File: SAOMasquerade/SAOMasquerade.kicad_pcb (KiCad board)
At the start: 2 copper layers, 31.8 x 35.6 mm, 20 parts, among them Q1 BSS138, SW1 SW_DIP_x07, U1 CH32V003FxPx, U2 74LVC1G86, U3 74LVC1G38, X1 SAO, X2 BADGE

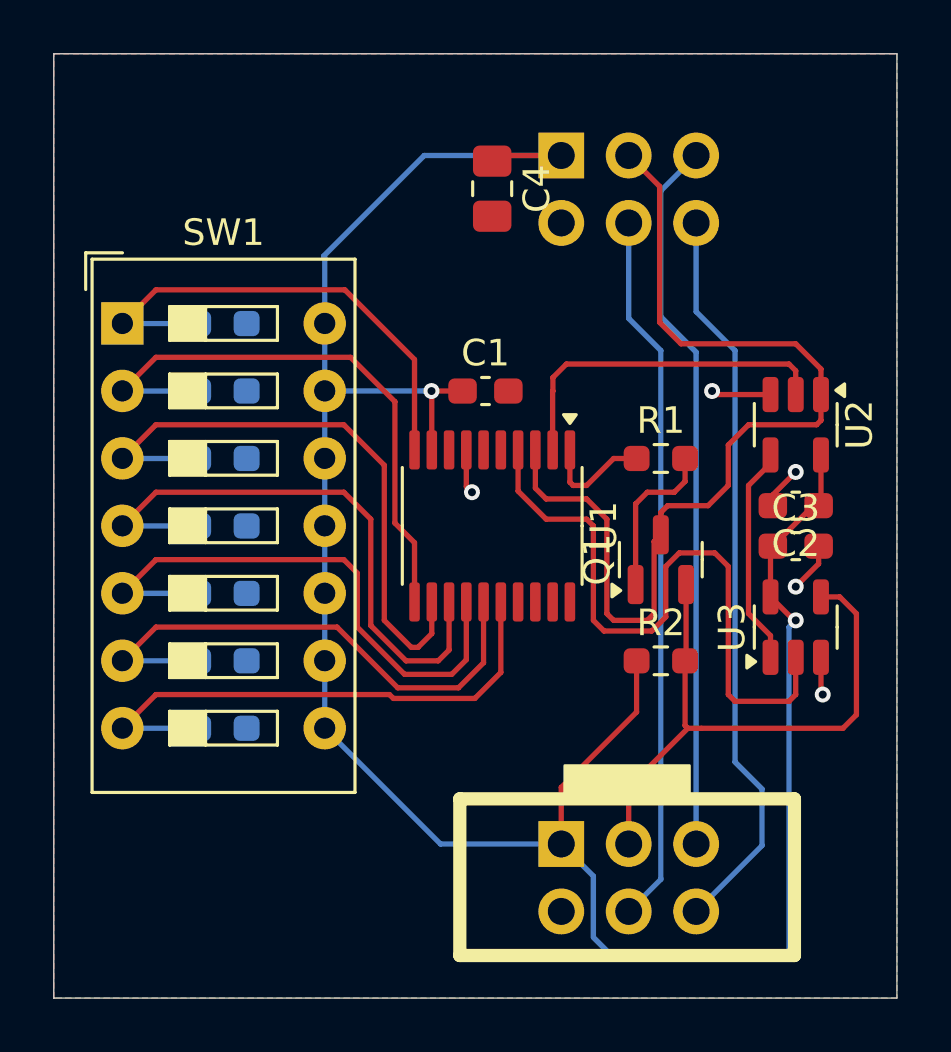
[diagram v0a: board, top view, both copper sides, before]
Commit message: Updating schematic to use analog switch instead of open drain NAND
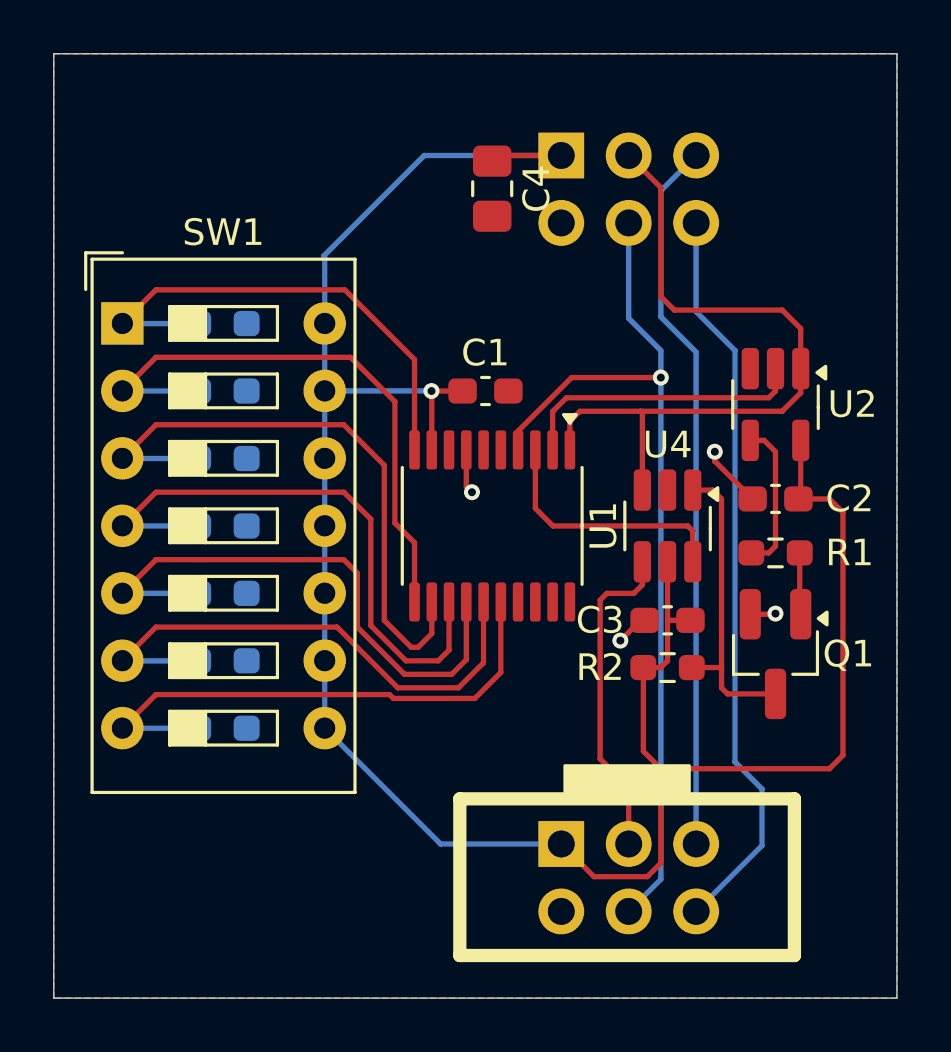
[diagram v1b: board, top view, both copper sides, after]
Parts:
- removed U3: 74LVC1G38, Package_TO_SOT_SMD:SOT-23-5
- added U4: 74LVC1G3157, Package_TO_SOT_SMD:SOT-23-6_Handsoldering, F.Cu at (153.9, 114.3)
- Q1: footprint Package_TO_SOT_SMD:SOT-23 -> Package_TO_SOT_SMD:SOT-23_Handsoldering
- U2: footprint Package_TO_SOT_SMD:SOT-23-5 -> Package_TO_SOT_SMD:SOT-23-5_HandSoldering
- moved Q1 5.59 mm to (158.0, 119.1), turned to -90 degrees
- moved R1 5.59 mm to (158.0, 115.3)
- moved C3 5.58 mm to (153.9, 117.9), turned to 180 degrees
- moved U2 1.08 mm to (158.0, 109.7)
- moved C2 0.80 mm to (158.0, 113.3)
- moved R2 0.36 mm to (153.9, 119.6)
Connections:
- net /XOR_IN renamed /~{XOR_IN}
- Q1 pad 2: /SDA_MODIFIED -> GND
- Q1 pad 3: /SDA_UNMODIFIED -> Net-(Q1-D)
- R1 pad 1: /SDA_BYPASS -> Net-(R1-Pad1)
- R2 pad 2: /SDA_MODIFIED -> Net-(Q1-D)
- U1 pad 1: /SDA_BYPASS -> /SDA_UNMODIFIED
- U1 pad 3: /SDA_UNMODIFIED -> /SDA_BYPASS
- U1 pad 4: /MODIFIED_OE -> /SCL
- U2 pad 4: Net-(U2-Pad4) -> Net-(R1-Pad1)
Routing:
- net /MODIFIED_OE: track 25.3 -> 0.00 mm
- net Net-(Q1-D): track 0.00 -> 11.6 mm
- net /SDA_UNMODIFIED: track 37.9 -> 27.2 mm
- net /SDA_MODIFIED: track 22.7 -> 12.3 mm
- net Net-(U2-Pad4): track 8.31 -> 0.00 mm
- net /SCL: track 26.9 -> 33.8 mm, vias 0 -> 1
- net Net-(R1-Pad1): track 0.00 -> 5.70 mm
- net /SDA_BYPASS: track 4.20 -> 9.64 mm
- net Net-(Q1-G): track 6.11 -> 2.33 mm
- net GND: track 8.87 -> 6.24 mm, vias 5 -> 4
- net /~{XOR_IN}: track 13.1 -> 11.0 mm
- net +3V3: track 89.1 -> 87.2 mm, vias 2 -> 1

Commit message: Adding debuggability
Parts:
- added J1: Conn_01x04, Connector_PinHeader_2.54mm:PinHeader_1x04_P2.54mm_Vertical, F.Cu at (141.2, 130.0)
- added J2: Conn_01x03, Connector_PinHeader_2.54mm:PinHeader_1x03_P2.54mm_Vertical, F.Cu at (141.2, 98.6)
- R1: value 4.7K -> 1K
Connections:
- U1 pad 1: /SDA_UNMODIFIED -> unconnected-(U1-PD4-Pad1)
- U1 pad 17: unconnected-(U1-PC7-Pad17) -> /~{XOR_IN}
- U1 pad 18: unconnected-(U1-PD1-Pad18) -> /SWIO
- U1 pad 19: unconnected-(U1-PD2-Pad19) -> /SDA_UNMODIFIED
- U1 pad 2: /~{XOR_IN} -> /UART_TX
- U1 pad 20: unconnected-(U1-PD3-Pad20) -> /SDA_BYPASS
- U1 pad 3: /SDA_BYPASS -> /UART_RX
- U1 pad 4: /SCL -> /~{RESET}
- U1 pad 5: unconnected-(U1-PA1-Pad5) -> /SCL
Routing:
- net /~{RESET}: track 0.00 -> 24.6 mm, vias 0 -> 2
- net /UART_RX: track 0.00 -> 21.5 mm, vias 0 -> 2
- net /UART_TX: track 0.00 -> 17.3 mm, vias 0 -> 2
- net /SWIO: track 0.00 -> 17.1 mm
- net +3V3: track 87.2 -> 94.2 mm
- net /~{XOR_IN}: track 11.0 -> 16.4 mm
- net /SDA_UNMODIFIED: track 27.2 -> 29.6 mm
- net /SCL: track 33.8 -> 35.1 mm
- net /SDA_BYPASS: track 9.64 -> 8.51 mm
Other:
- board text added: "3.3V"
- board text added: "GND"
- board text added: "RX_I"
- board text added: "SAOMasquerade Test Board by rglenn 2024-11-23"
- board text added: "SWIO"
- board text added: "TX_O"
- board text added: "~{RST}"
